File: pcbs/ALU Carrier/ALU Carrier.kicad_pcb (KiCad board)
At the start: 2 copper layers, 21 parts, among them J1001 Conn_02x20_Odd_Even, J1002 Conn_02x20_Odd_Even, U2001 74HC138, U2002 74HC14, U2003 74HC08

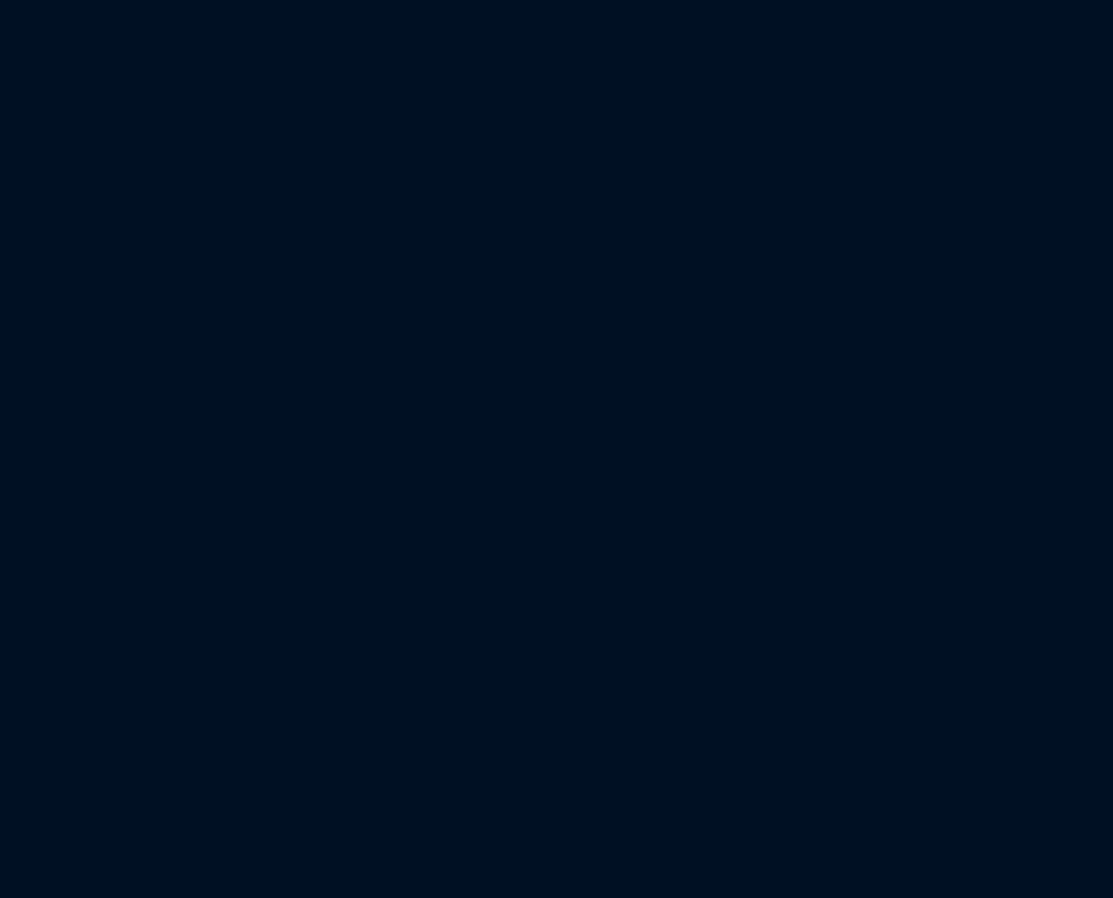
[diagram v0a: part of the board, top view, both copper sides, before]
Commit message: Adding the adder
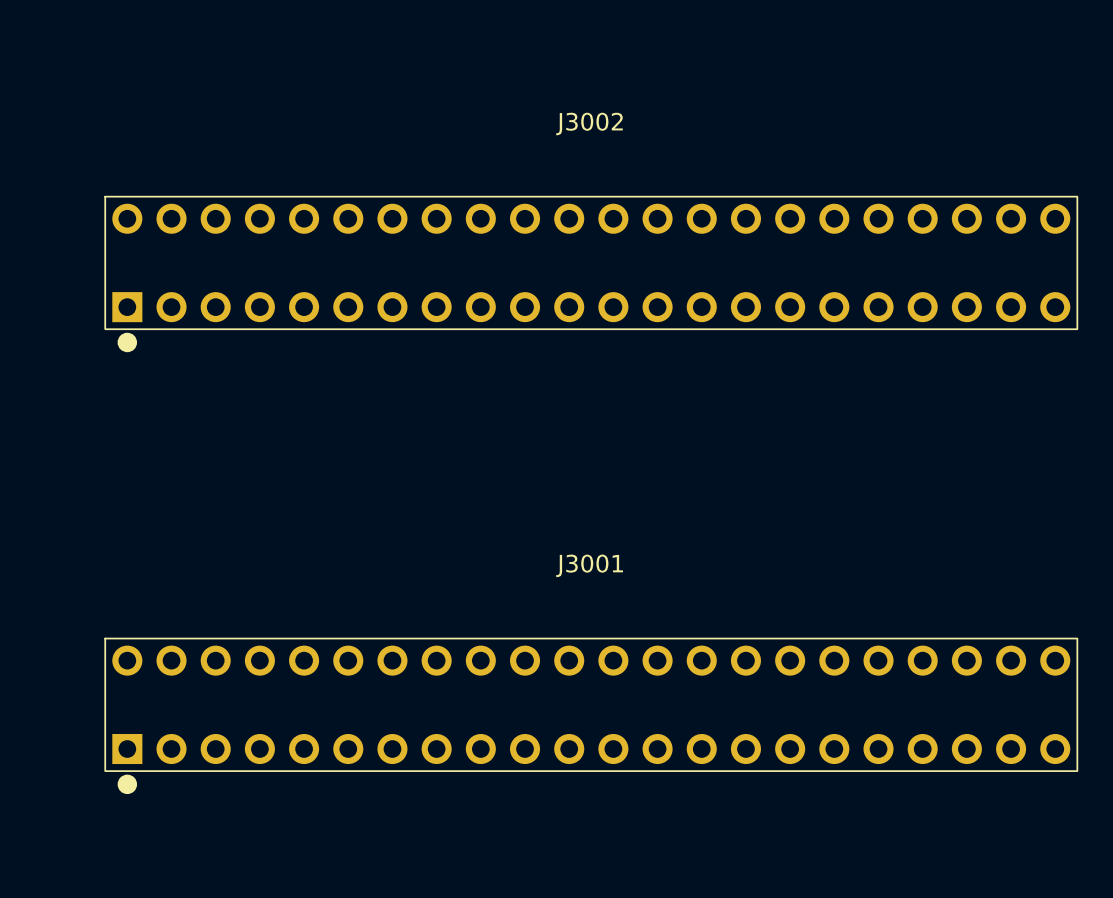
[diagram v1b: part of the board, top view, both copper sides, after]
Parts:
- added J3001: ~, BoardEdgeConnectors:TE-5530843-4-Mount, F.Cu at (177.8, 254.0)
- added J3002: ~, BoardEdgeConnectors:TE-5530843-4-Mount, F.Cu at (177.8, 228.6)
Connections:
- net /Cycle0 renamed /Instruction Decoder/Cycle0
- net /Cycle1 renamed /Instruction Decoder/Cycle1
- net /Cycle4 renamed /Instruction Decoder/Cycle4
- net /I10 renamed /Instruction Decoder/I10
- net /I11 renamed /Instruction Decoder/I11
- net /I12 renamed /Instruction Decoder/I12
- net /I13 renamed /Instruction Decoder/I13
- net /I14 renamed /Instruction Decoder/I14
- net /I15 renamed /Instruction Decoder/I15
- net /I4 renamed /Instruction Decoder/I4
- net /I5 renamed /Instruction Decoder/I5
- net /I6 renamed /Instruction Decoder/I6
- net /I7 renamed /Instruction Decoder/I7
- net /I8 renamed /Instruction Decoder/I8
- net /I9 renamed /Instruction Decoder/I9
- net /Instruction Decoder/~{ADD} renamed /Adder Subtractor/~{ADD}
- net /Instruction Decoder/~{SUB} renamed /Adder Subtractor/~{SUB}
- J1001 pad 19: /B0 -> /Adder Subtractor/B0
- J1001 pad 20: /B1 -> /Adder Subtractor/B1
- J1001 pad 21: /B2 -> /Adder Subtractor/B2
- J1001 pad 22: /B3 -> /Adder Subtractor/B3
- J1001 pad 23: /B4 -> /Adder Subtractor/B4
- J1001 pad 24: /B5 -> /Adder Subtractor/B5
- J1001 pad 25: /B6 -> /Adder Subtractor/B6
- J1001 pad 26: /B7 -> /Adder Subtractor/B7
- J1001 pad 27: /B8 -> /Adder Subtractor/B8
- J1001 pad 28: /B9 -> /Adder Subtractor/B9
- J1001 pad 29: /B10 -> /Adder Subtractor/B10
- J1001 pad 30: /B11 -> /Adder Subtractor/B11
- J1001 pad 31: /B12 -> /Adder Subtractor/B12
- J1001 pad 32: /B13 -> /Adder Subtractor/B13
- J1001 pad 33: /B14 -> /Adder Subtractor/B14
- J1001 pad 34: /B15 -> /Adder Subtractor/B15
- J1002 pad 17: /I0 -> /Instruction Decoder/I0
- J1002 pad 18: /I1 -> /Instruction Decoder/I1
- J1002 pad 19: /I2 -> /Instruction Decoder/I2
- J1002 pad 20: /I3 -> /Instruction Decoder/I3
- J1002 pad 35: /Cycle2 -> /Instruction Decoder/Cycle2
- J1002 pad 36: /Cycle3 -> /Instruction Decoder/Cycle3

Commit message: Working...
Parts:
- added J4001: ~, BoardEdgeConnectors:TE-5530843-4-Mount, F.Cu at (176.5, 177.8)
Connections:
- net /Instruction Decoder/~{Compare} renamed /Comparator/~{Compare}
- J1001 pad 19: /Adder Subtractor/B0 -> /B0
- J1001 pad 20: /Adder Subtractor/B1 -> /B1
- J1001 pad 21: /Adder Subtractor/B2 -> /B2
- J1001 pad 22: /Adder Subtractor/B3 -> /B3
- J1001 pad 23: /Adder Subtractor/B4 -> /B4
- J1001 pad 24: /Adder Subtractor/B5 -> /B5
- J1001 pad 25: /Adder Subtractor/B6 -> /B6
- J1001 pad 26: /Adder Subtractor/B7 -> /B7
- J1001 pad 27: /Adder Subtractor/B8 -> /B8
- J1001 pad 28: /Adder Subtractor/B9 -> /B9
- J1001 pad 29: /Adder Subtractor/B10 -> /B10
- J1001 pad 30: /Adder Subtractor/B11 -> /B11
- J1001 pad 31: /Adder Subtractor/B12 -> /B12
- J1001 pad 32: /Adder Subtractor/B13 -> /B13
- J1001 pad 33: /Adder Subtractor/B14 -> /B14
- J1001 pad 34: /Adder Subtractor/B15 -> /B15

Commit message: Roughing out
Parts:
- added J5001: ~, BoardEdgeConnectors:TE-5530843-4-Mount, F.Cu at (177.8, 101.6)
- added J5002: ~, BoardEdgeConnectors:TE-5530843-4-Mount, F.Cu at (177.8, 127.0)
- added J6001: ~, BoardEdgeConnectors:TE-5530843-4-Mount, F.Cu at (177.8, 50.8)
- added J6002: ~, BoardEdgeConnectors:TE-5530843-4-Mount, F.Cu at (177.8, 25.4)
- added U6001: 74HC14, Package_SO:SOIC-14_3.9x8.7mm_P1.27mm, F.Cu at (144.8, 38.1)
- moved J4001 1.27 mm to (177.8, 177.8)
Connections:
- net /Instruction Decoder/~{Barrel} renamed /Barrel Shifter/~{Shift}
- J1001 pad 19: /B0 -> /Adder Subtractor/B0
- J1001 pad 20: /B1 -> /Adder Subtractor/B1
- J1001 pad 21: /B2 -> /Adder Subtractor/B2
- J1001 pad 22: /B3 -> /Adder Subtractor/B3
- J1001 pad 23: /B4 -> /Adder Subtractor/B4
- J1001 pad 24: /B5 -> /Adder Subtractor/B5
- J1001 pad 25: /B6 -> /Adder Subtractor/B6
- J1001 pad 26: /B7 -> /Adder Subtractor/B7
- J1001 pad 27: /B8 -> /Adder Subtractor/B8
- J1001 pad 28: /B9 -> /Adder Subtractor/B9
- J1001 pad 29: /B10 -> /Adder Subtractor/B10
- J1001 pad 30: /B11 -> /Adder Subtractor/B11
- J1001 pad 31: /B12 -> /Adder Subtractor/B12
- J1001 pad 32: /B13 -> /Adder Subtractor/B13
- J1001 pad 33: /B14 -> /Adder Subtractor/B14
- J1001 pad 34: /B15 -> /Adder Subtractor/B15
- J4001 pad A11: /Comparator/B0 -> /Adder Subtractor/B0
- J4001 pad A12: /Comparator/B2 -> /Adder Subtractor/B2
- J4001 pad A13: /Comparator/B4 -> /Adder Subtractor/B4
- J4001 pad A14: /Comparator/B6 -> /Adder Subtractor/B6
- J4001 pad A15: /Comparator/B8 -> /Adder Subtractor/B8
- J4001 pad A16: /Comparator/B10 -> /Adder Subtractor/B10
- J4001 pad A17: /Comparator/B12 -> /Adder Subtractor/B12
- J4001 pad A18: /Comparator/B14 -> /Adder Subtractor/B14
- J4001 pad B11: /Comparator/B1 -> /Adder Subtractor/B1
- J4001 pad B12: /Comparator/B3 -> /Adder Subtractor/B3
- J4001 pad B13: /Comparator/B5 -> /Adder Subtractor/B5
- J4001 pad B14: /Comparator/B7 -> /Adder Subtractor/B7
- J4001 pad B15: /Comparator/B9 -> /Adder Subtractor/B9
- J4001 pad B16: /Comparator/B11 -> /Adder Subtractor/B11
- J4001 pad B17: /Comparator/B13 -> /Adder Subtractor/B13
- J4001 pad B18: /Comparator/B15 -> /Adder Subtractor/B15

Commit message: Fix indicators
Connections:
- D2001 pad 1: GND -> Net-(D2001-K)
- D2001 pad 2: Net-(D2001-A) -> +5V
- D2002 pad 1: GND -> Net-(D2002-K)
- D2002 pad 2: Net-(D2002-A) -> +5V
- D2003 pad 1: GND -> Net-(D2003-K)
- D2003 pad 2: Net-(D2003-A) -> +5V
- D2004 pad 1: GND -> Net-(D2004-K)
- D2004 pad 2: Net-(D2004-A) -> +5V
- D2005 pad 1: GND -> Net-(D2005-K)
- D2005 pad 2: Net-(D2005-A) -> +5V
- D2006 pad 1: GND -> Net-(D2006-K)
- D2006 pad 2: Net-(D2006-A) -> +5V
- D2007 pad 1: GND -> Net-(D2007-K)
- D2007 pad 2: Net-(D2007-A) -> +5V
- D2008 pad 1: GND -> Net-(D2008-K)
- D2008 pad 2: Net-(D2008-A) -> +5V
- R2001 pad 1: Net-(D2001-A) -> Net-(D2001-K)
- R2002 pad 1: Net-(D2002-A) -> Net-(D2002-K)
- R2003 pad 1: Net-(D2003-A) -> Net-(D2003-K)
- R2004 pad 1: Net-(D2004-A) -> Net-(D2004-K)
- R2005 pad 1: Net-(D2005-A) -> Net-(D2005-K)
- R2006 pad 1: Net-(D2006-A) -> Net-(D2006-K)
- R2007 pad 1: Net-(D2007-A) -> Net-(D2007-K)
- R2008 pad 1: Net-(D2008-A) -> Net-(D2008-K)
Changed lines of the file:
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@@
 	(net 0 "")
 	(net 1 "GND")
-	(net 2 "Net-(D2001-A)")
-	(net 3 "Net-(D2002-A)")
-	(net 4 "Net-(D2003-A)")
-	(net 5 "Net-(D2004-A)")
-	(net 6 "Net-(D2005-A)")
-	(net 7 "Net-(D2006-A)")
-	(net 8 "Net-(D2007-A)")
-	(net 9 "Net-(D2008-A)")
+	(net 2 "Net-(D2001-K)")
+	(net 3 "Net-(D2002-K)")
+	(net 4 "Net-(D2003-K)")
+	(net 5 "Net-(D2004-K)")
+	(net 6 "Net-(D2005-K)")
+	(net 7 "Net-(D2006-K)")
+	(net 8 "Net-(D2007-K)")
+	(net 9 "Net-(D2008-K)")
 	(net 10 "unconnected-(J1001-Pin_35-Pad35)")
 	(net 11 "/A1")
@@
 			(layers "F.Cu" "F.Paste" "F.Mask")
 			(roundrect_rratio 0.25)
-			(net 2 "Net-(D2001-A)")
+			(net 2 "Net-(D2001-K)")
 			(pintype "passive")
 		)
@@
 			(layers "F.Cu" "F.Paste" "F.Mask")
 			(roundrect_rratio 0.25)
-			(net 7 "Net-(D2006-A)")
+			(net 7 "Net-(D2006-K)")
 			(pintype "passive")
 		)
@@
 			(layers "F.Cu" "F.Paste" "F.Mask")
 			(roundrect_rratio 0.25)
-			(net 6 "Net-(D2005-A)")
+			(net 6 "Net-(D2005-K)")
 			(pintype "passive")
 		)
@@
 			(layers "F.Cu" "F.Paste" "F.Mask")
 			(roundrect_rratio 0.25)
-			(net 8 "Net-(D2007-A)")
+			(net 8 "Net-(D2007-K)")
 			(pintype "passive")
 		)
@@
 			(layers "F.Cu" "F.Paste" "F.Mask")
 			(roundrect_rratio 0.25)
-			(net 1 "GND")
+			(net 3 "Net-(D2002-K)")
 			(pinfunction "K")
 			(pintype "passive")
@@
 			(layers "F.Cu" "F.Paste" "F.Mask")
 			(roundrect_rratio 0.25)
-			(net 3 "Net-(D2002-A)")
+			(net 20 "+5V")
 			(pinfunction "A")
 			(pintype "passive")
@@
 			(layers "F.Cu" "F.Paste" "F.Mask")
 			(roundrect_rratio 0.25)
-			(net 1 "GND")
+			(net 5 "Net-(D2004-K)")
 			(pinfunction "K")
 			(pintype "passive")
@@
 			(layers "F.Cu" "F.Paste" "F.Mask")
 			(roundrect_rratio 0.25)
-			(net 5 "Net-(D2004-A)")
+			(net 20 "+5V")
 			(pinfunction "A")
 			(pintype "passive")
@@
 			(layers "F.Cu" "F.Paste" "F.Mask")
 			(roundrect_rratio 0.25)
-			(net 1 "GND")
+			(net 8 "Net-(D2007-K)")
 			(pinfunction "K")
 			(pintype "passive")
@@
 			(layers "F.Cu" "F.Paste" "F.Mask")
 			(roundrect_rratio 0.25)
-			(net 8 "Net-(D2007-A)")
+			(net 20 "+5V")
 			(pinfunction "A")
 			(pintype "passive")
@@
 			(layers "F.Cu" "F.Paste" "F.Mask")
 			(roundrect_rratio 0.25)
-			(net 1 "GND")
+			(net 9 "Net-(D2008-K)")
 			(pinfunction "K")
 			(pintype "passive")
@@
 			(layers "F.Cu" "F.Paste" "F.Mask")
 			(roundrect_rratio 0.25)
-			(net 9 "Net-(D2008-A)")
+			(net 20 "+5V")
 			(pinfunction "A")
 			(pintype "passive")
@@
 			(layers "F.Cu" "F.Paste" "F.Mask")
 			(roundrect_rratio 0.25)
-			(net 1 "GND")
+			(net 7 "Net-(D2006-K)")
 			(pinfunction "K")
 			(pintype "passive")
@@
 			(layers "F.Cu" "F.Paste" "F.Mask")
 			(roundrect_rratio 0.25)
-			(net 7 "Net-(D2006-A)")
+			(net 20 "+5V")
 			(pinfunction "A")
 			(pintype "passive")
@@
 			(layers "F.Cu" "F.Paste" "F.Mask")
 			(roundrect_rratio 0.25)
-			(net 1 "GND")
+			(net 2 "Net-(D2001-K)")
 			(pinfunction "K")
 			(pintype "passive")
@@
 			(layers "F.Cu" "F.Paste" "F.Mask")
 			(roundrect_rratio 0.25)
-			(net 2 "Net-(D2001-A)")
+			(net 20 "+5V")
 			(pinfunction "A")
 			(pintype "passive")
@@
 			(layers "F.Cu" "F.Paste" "F.Mask")
 			(roundrect_rratio 0.25)
-			(net 9 "Net-(D2008-A)")
+			(net 9 "Net-(D2008-K)")
 			(pintype "passive")
 		)
@@
 			(layers "F.Cu" "F.Paste" "F.Mask")
 			(roundrect_rratio 0.25)
-			(net 3 "Net-(D2002-A)")
+			(net 3 "Net-(D2002-K)")
 			(pintype "passive")
 		)
@@
 			(layers "F.Cu" "F.Paste" "F.Mask")
 			(roundrect_rratio 0.25)
-			(net 4 "Net-(D2003-A)")
+			(net 4 "Net-(D2003-K)")
 			(pintype "passive")
 		)
@@
 			(layers "F.Cu" "F.Paste" "F.Mask")
 			(roundrect_rratio 0.25)
-			(net 5 "Net-(D2004-A)")
+			(net 5 "Net-(D2004-K)")
 			(pintype "passive")
 		)
@@
 			(layers "F.Cu" "F.Paste" "F.Mask")
 			(roundrect_rratio 0.25)
-			(net 1 "GND")
+			(net 6 "Net-(D2005-K)")
 			(pinfunction "K")
 			(pintype "passive")
@@
 			(layers "F.Cu" "F.Paste" "F.Mask")
 			(roundrect_rratio 0.25)
-			(net 6 "Net-(D2005-A)")
+			(net 20 "+5V")
 			(pinfunction "A")
 			(pintype "passive")
@@
 			(layers "F.Cu" "F.Paste" "F.Mask")
 			(roundrect_rratio 0.25)
-			(net 1 "GND")
+			(net 4 "Net-(D2003-K)")
 			(pinfunction "K")
 			(pintype "passive")
@@
 			(layers "F.Cu" "F.Paste" "F.Mask")
 			(roundrect_rratio 0.25)
-			(net 4 "Net-(D2003-A)")
+			(net 20 "+5V")
 			(pinfunction "A")
 			(pintype "passive")

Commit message: Roughing out some layout
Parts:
- removed U2002: 74HC14, Package_SO:SOIC-14_3.9x8.7mm_P1.27mm
- removed U2003: 74HC08, Package_SO:SOIC-14_3.9x8.7mm_P1.27mm
- added D8001: WHITE, LED_SMD:LED_0603_1608Metric, F.Cu at (251.1, 147.4)
- added D8002: WHITE, LED_SMD:LED_0603_1608Metric, F.Cu at (251.1, 150.0)
- added D8003: WHITE, LED_SMD:LED_0603_1608Metric, F.Cu at (251.1, 152.6)
- added D8004: WHITE, LED_SMD:LED_0603_1608Metric, F.Cu at (251.1, 155.2)
- added D8005: WHITE, LED_SMD:LED_0603_1608Metric, F.Cu at (251.1, 157.8)
- added D8006: WHITE, LED_SMD:LED_0603_1608Metric, F.Cu at (251.1, 160.4)
- added D8007: WHITE, LED_SMD:LED_0603_1608Metric, F.Cu at (255.1, 147.4)
- added D8008: WHITE, LED_SMD:LED_0603_1608Metric, F.Cu at (255.1, 150.0)
- added D8009: WHITE, LED_SMD:LED_0603_1608Metric, F.Cu at (255.1, 152.6)
- added D8010: WHITE, LED_SMD:LED_0603_1608Metric, F.Cu at (255.1, 155.2)
- added D8011: WHITE, LED_SMD:LED_0603_1608Metric, F.Cu at (255.1, 157.8)
- added D8012: WHITE, LED_SMD:LED_0603_1608Metric, F.Cu at (255.1, 160.4)
- added D8013: WHITE, LED_SMD:LED_0603_1608Metric, F.Cu at (259.2, 147.4)
- added D8014: WHITE, LED_SMD:LED_0603_1608Metric, F.Cu at (259.2, 150.0)
- added D8015: WHITE, LED_SMD:LED_0603_1608Metric, F.Cu at (259.2, 152.6)
- added D8016: WHITE, LED_SMD:LED_0603_1608Metric, F.Cu at (259.2, 155.2)
- added D8017: Blue, LED_SMD:LED_0603_1608Metric, F.Cu at (259.2, 157.8)
- added R8001: 4k7, Resistor_SMD:R_0603_1608Metric, F.Cu at (263.2, 147.4)
- added R8002: 4k7, Resistor_SMD:R_0603_1608Metric, F.Cu at (263.2, 149.9)
- added R8003: 4k7, Resistor_SMD:R_0603_1608Metric, F.Cu at (263.2, 152.4)
- added R8004: 4k7, Resistor_SMD:R_0603_1608Metric, F.Cu at (263.2, 154.9)
- added R8005: 4k7, Resistor_SMD:R_0603_1608Metric, F.Cu at (263.2, 157.4)
- added R8006: 4k7, Resistor_SMD:R_0603_1608Metric, F.Cu at (263.2, 159.9)
- added R8007: 4k7, Resistor_SMD:R_0603_1608Metric, F.Cu at (267.2, 147.4)
- added R8008: 4k7, Resistor_SMD:R_0603_1608Metric, F.Cu at (267.2, 149.9)
- added R8009: 4k7, Resistor_SMD:R_0603_1608Metric, F.Cu at (267.2, 152.4)
- added R8010: 4k7, Resistor_SMD:R_0603_1608Metric, F.Cu at (267.2, 154.9)
- added R8011: 4k7, Resistor_SMD:R_0603_1608Metric, F.Cu at (267.2, 157.4)
- added R8012: 4k7, Resistor_SMD:R_0603_1608Metric, F.Cu at (267.2, 159.9)
- added R8013: 4k7, Resistor_SMD:R_0603_1608Metric, F.Cu at (271.2, 147.4)
- added R8014: 4k7, Resistor_SMD:R_0603_1608Metric, F.Cu at (271.2, 149.9)
- added R8015: 4k7, Resistor_SMD:R_0603_1608Metric, F.Cu at (271.2, 152.4)
- added R8016: 4k7, Resistor_SMD:R_0603_1608Metric, F.Cu at (271.2, 154.9)
- added R8017: 4k7, Resistor_SMD:R_0603_1608Metric, F.Cu at (271.2, 157.4)
- added U7001: 74HC14, Package_SO:SOIC-14_3.9x8.7mm_P1.27mm, F.Cu at (67.7, 123.2)
- added U7002: 74HC08, Package_SO:SOIC-14_3.9x8.7mm_P1.27mm, F.Cu at (76.1, 123.2)
- added U8001: 74HC245, Package_SO:SOIC-20W_7.5x12.8mm_P1.27mm, F.Cu at (255.5, 138.9)
- added U8002: 74HC245, Package_SO:SOIC-20W_7.5x12.8mm_P1.27mm, F.Cu at (268.4, 138.9)
- moved U6001 55.9 mm to (88.9, 38.1)
- moved J1001 25.4 mm to (25.4, 152.4)
- moved J1002 25.4 mm to (25.4, 228.6)
- moved J4001 12.7 mm to (177.8, 165.1)
- moved J6001 12.7 mm to (177.8, 63.5)
- moved J6002 12.7 mm to (177.8, 38.1)
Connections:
- net /Adder Subtractor/B0 renamed /B0
- net /Adder Subtractor/B1 renamed /B1
- net /Adder Subtractor/B10 renamed /B10
- net /Adder Subtractor/B11 renamed /B11
- net /Adder Subtractor/B12 renamed /B12
- net /Adder Subtractor/B13 renamed /B13
- net /Adder Subtractor/B14 renamed /B14
- net /Adder Subtractor/B15 renamed /B15
- net /Adder Subtractor/B2 renamed /B2
- net /Adder Subtractor/B3 renamed /B3
- net /Adder Subtractor/B4 renamed /B4
- net /Adder Subtractor/B5 renamed /B5
- net /Adder Subtractor/B6 renamed /B6
- net /Adder Subtractor/B7 renamed /B7
- net /Adder Subtractor/B8 renamed /B8
- net /Adder Subtractor/B9 renamed /B9
- net /Instruction Decoder/Cycle0 renamed /Enabler/Cycle0
- net /Instruction Decoder/Cycle1 renamed /Enabler/Cycle1
- net /Instruction Decoder/Cycle4 renamed /Enabler/Cycle4
- J1002 pad 35: /Instruction Decoder/Cycle2 -> /Enabler/Cycle2
- J1002 pad 36: /Instruction Decoder/Cycle3 -> /Enabler/Cycle3
- U2001 pad 5: /Instruction Decoder/~{Enable} -> /Enabler/~{Enable}
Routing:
- net /B1: track 0.00 -> 242.1 mm
- net /A1: track 0.00 -> 199.8 mm
- net /B3: track 0.00 -> 191.0 mm
- net /B2: track 0.00 -> 187.9 mm
- net /A0: track 0.00 -> 178.6 mm
- net /B15: track 0.00 -> 174.9 mm
- net /B0: track 0.00 -> 174.5 mm
- net /A2: track 0.00 -> 173.2 mm
- net /B13: track 0.00 -> 171.7 mm
- net /B14: track 0.00 -> 152.0 mm
- net /B12: track 0.00 -> 148.9 mm
- net /A15: track 0.00 -> 136.0 mm
- net /A13: track 0.00 -> 126.5 mm
- net /A11: track 0.00 -> 117.0 mm
- net /B11: track 0.00 -> 114.6 mm
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
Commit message: Some routing
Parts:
- moved U8001 75.8 mm to (241.3, 213.4)
- moved U8002 75.4 mm to (256.5, 213.4)
- moved U6001 69.4 mm to (142.2, 82.5)
- moved J3001 25.4 mm to (177.8, 228.6)
- moved J3002 25.4 mm to (177.8, 203.2)
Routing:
- net /A14: track 90.7 -> 320.7 mm
- net /A7: track 97.9 -> 321.4 mm
- net /A5: track 88.4 -> 306.1 mm
- net /A10: track 78.0 -> 292.8 mm
- net /A6: track 78.0 -> 290.2 mm
- net /A8: track 71.6 -> 278.8 mm
- net /A4: track 71.6 -> 276.3 mm
- net /A3: track 92.5 -> 279.4 mm
- net /A13: track 126.5 -> 310.3 mm
- net /A9: track 107.5 -> 283.6 mm
- net /A15: track 136.0 -> 302.0 mm
- net /B7: track 54.2 -> 211.0 mm
- net /B6: track 44.1 -> 197.0 mm
- net /B5: track 51.1 -> 202.1 mm
- net /B4: track 40.9 -> 181.8 mm
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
